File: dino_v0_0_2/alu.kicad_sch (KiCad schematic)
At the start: 20 parts, among them U38 74F382N, U40 74F382N, U45 74LS373, U46 74LS373, U47 74LS373, U48 74LS157, U49 74LS273, U50 74LS02, U52 74LS02, U53 74LS08

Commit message: feat: Phase F/F+ ISA: 174 instructions, timing fixes, and robust tooling
This commit integrates Phase F and F+ of the ISA, expanding the instruction set to 174 instructions. This includes:
- New conditional branch `JNC`, register-to-register moves, SP/PC readbacks and manipulation (HLSP/SPHL, INXSP/DCXSP).
- Indexed memory access (LDAX/STAX), SP-relative memory access (LDAS/STAS), and memory-indirect addressing (LDAM/STAM/JMPM, etc.) as a new addressing mode.
- Immediate ALU operations (ADI, SUI, ANI, etc.) and ALU results directly to B/C or memory.
- Compare-only instructions (CMP, TST).
- The `IN` opcode has been fully retired from the ISA as of 2026-08-27, and `0x00` confirmed as `NOP`.

Crucially, this commit resolves several critical hardware stability issues:
- Eliminated random machine halts by replacing a damaged `74HC14` (`U56`) and rewiring the reset chain.
- Fixed intermittent failures in `PROG_isasoak` due to ground bounce by starring GND/VCC connections (2026-09-01).
- Introduced microcode-level "SETTLE" states for 23 ALU instructions to ensure timing margins at 1.024MHz, resolving timing-dependent failures for instructions that load and consume operands in consecutive T-states.

The development tooling has also been significantly improved for robustness and accuracy:
- The assembler (`asm.py`) now uses `microcode_gen.py` as the single source of truth for ISA definitions.
- New self-checking ISA tests (`PROG_isa` and variants) were developed, incorporating mutation testing to verify subtest efficacy and provide detailed diagnostic feedback for debugging marginality or hangs.
- The microcode generator enforces hardware constraints at build time (e.g., valid `cond` flag selections, preventing `src=ROM` `dst=RAM` conflicts that led to the `MVI` bug).
- The simulator (`progrom_gen.py`) accurately models `OUT` latching the bus and `dst=RAM` writing to the address bus, and refuses to guess undefined `FLAG_C` states after logic operations.
- The root `Makefile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
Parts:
- added C82: 0.1µF, symbol Device:C_Small
- added U77: 74LS157, symbol 74xx:74LS157
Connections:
- net +5V: now also C82.1, U77.16 (VCC)
- net FLAG_C: now also U77.2 (I0a)
- net FLAG_Z: now also U77.3 (I1a)
- net GND: now also C82.2, U77.10 (I1c), U77.11 (I0c), U77.13 (I1d), U77.14 (I0d), U77.15 (E), U77.5 (I0b), U77.6 (I1b), U77.8 (GND)
- new net COND_FLAG: U77.4 (Za)
- new net CW21: U77.1 (S)
- no-connect marks 6 -> 9
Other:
- moved on the sheet: U38, U45, U47

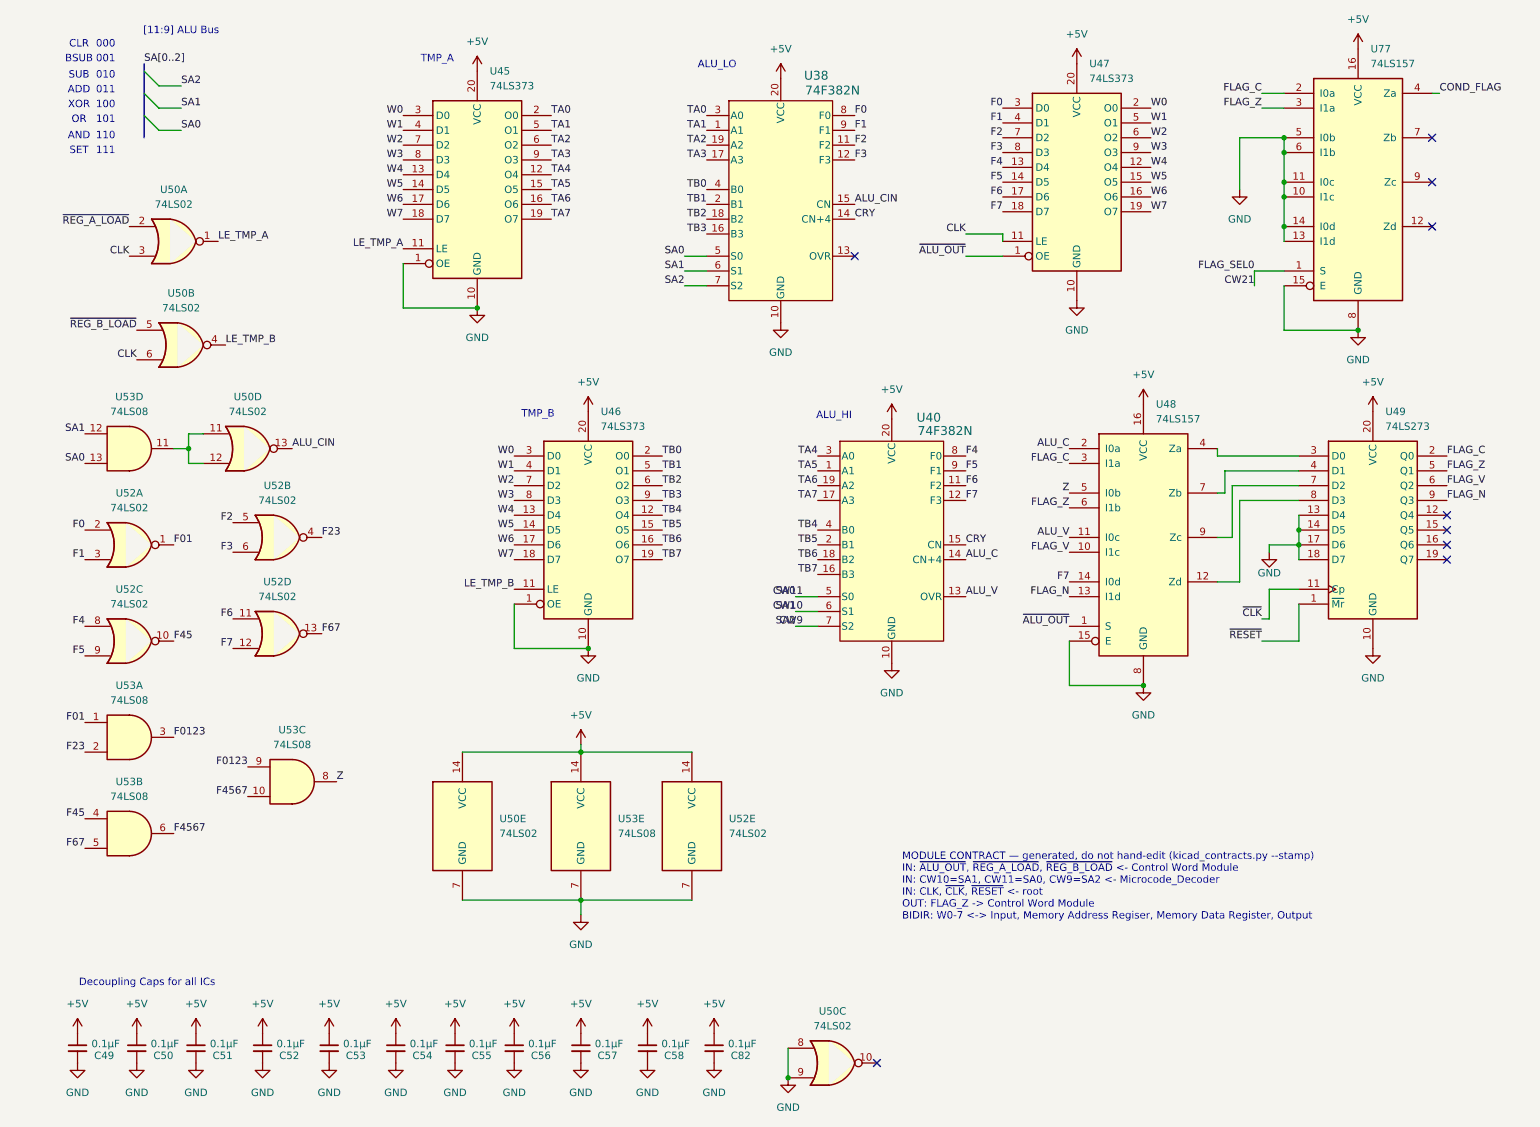
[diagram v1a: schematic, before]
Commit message: feat(kicad): footprints, power sheet, global labels, PCB draft
Every symbol gets a stock THT footprint (plain DIP, no sockets, so the
3D render shows ICs). New Power sheet: 24-pin ATX header for a picoPSU,
rails +5V/+3.3V/+12V/-12V/GND only; no -5V exists on any ATX unit since
2003, none drawn. PS_ON# on a 2-pin header.

Cross-sheet labels become global labels. KiCad joined nothing between
sheets before: 122 base names were split per sheet, ERC saw 90 undriven
inputs whose driver sat one sheet away, and the PCB ratsnest stopped at
every sheet boundary. Proof: KiCad's netlist after equals a name-join of
its netlist before plus the 15 CW alias pairs, pin for pin.

kicad_contracts took a node's sheet from the net name's /Sheet/ prefix;
global nets have none, so it emitted an empty contracts doc. Sheet now
comes from the component's own path; the doc regenerates with zero diff.

ERC 477 -> 2. Real fixes: ROM I/O pins input -> tri_state, '382 GND pin
power_out -> power_in, four orphan symbols rehomed to project lib `dino`,
one stub wire. 133 by-design warnings excluded by uuid ('245 readback on
counter Q, alias stubs, probe-point labels); the two left are bus
signals the peripheral bus sheet will consume.

PCB draft: 198 footprints placed per sheet, all pads netted, no tracks.

Co-Authored-By: Claude Fable 5.1 <noreply@anthropic.com>
Claude-Session: https://claude.ai/code/session_018irreFHb1xEykW5kCD26ow
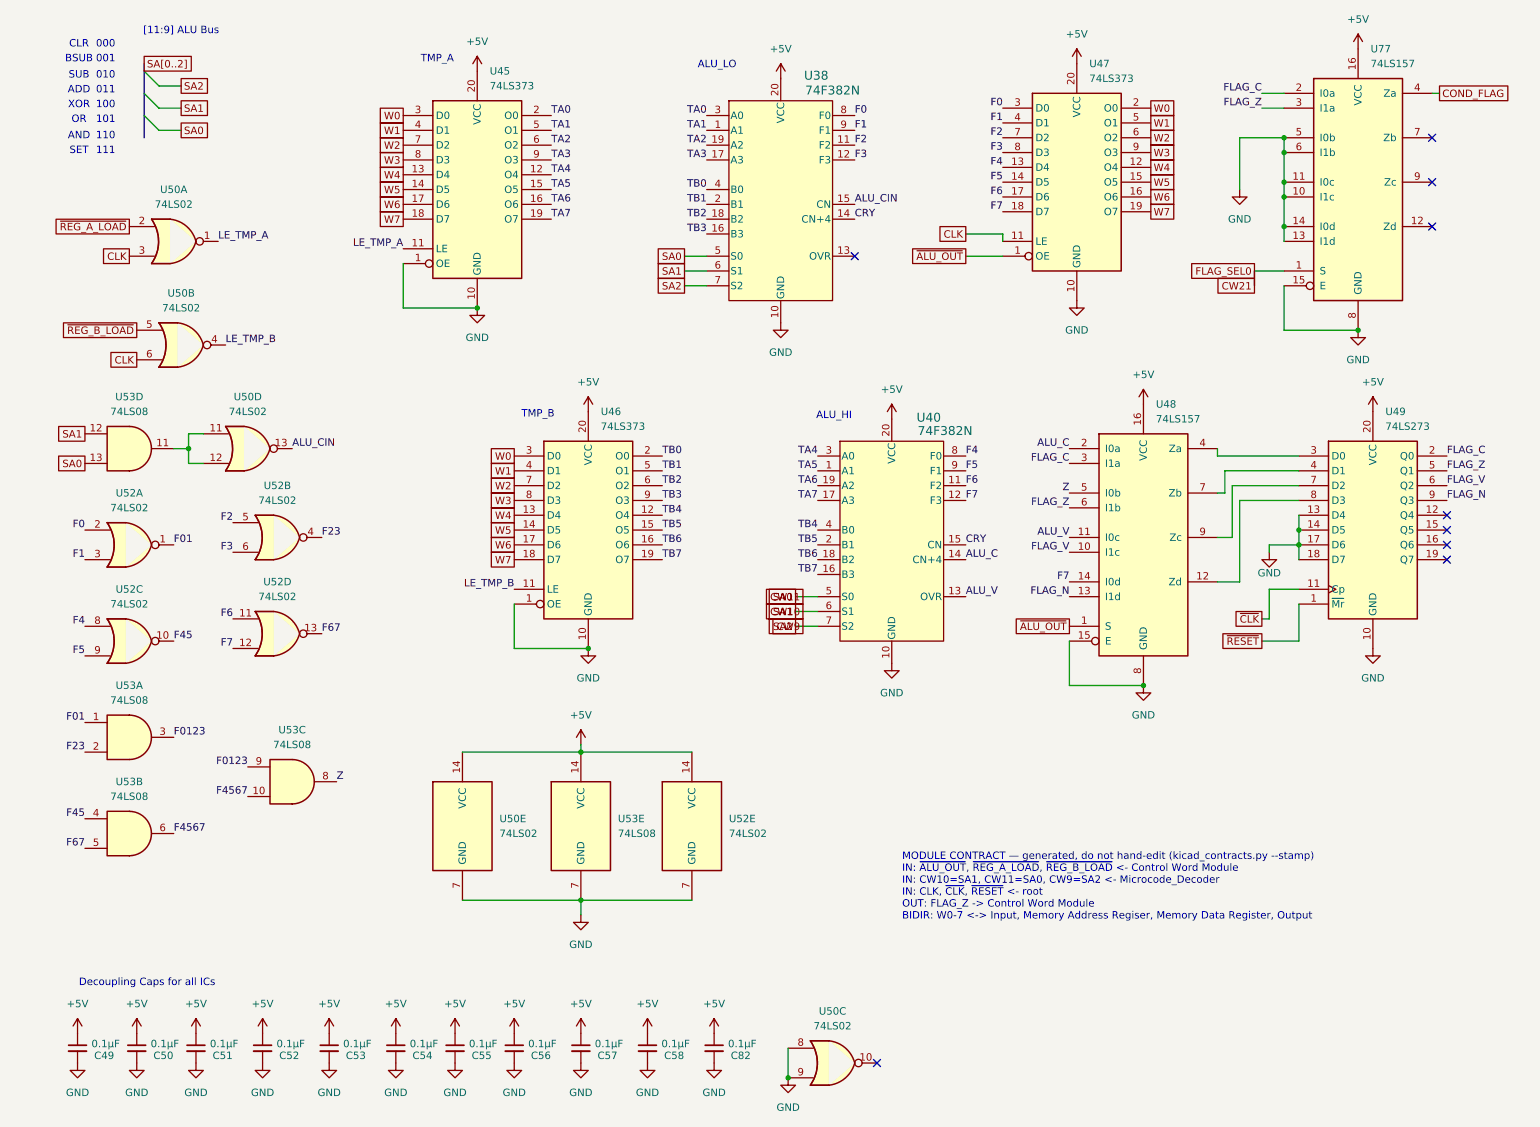
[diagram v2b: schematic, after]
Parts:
- C49, C50, C51, C52, C53, C54, C55, C56, C57, C58, C82: footprint (none) -> Capacitor_THT:C_Disc_D5.0mm_W2.5mm_P2.50mm
- U38, U40: footprint PDIP20_26P42X6P6_ONS -> Package_DIP:DIP-20_W7.62mm
- U45, U46, U47, U49: footprint (none) -> Package_DIP:DIP-20_W7.62mm
- U48, U77: footprint (none) -> Package_DIP:DIP-16_W7.62mm
- U50, U52, U53: footprint (none) -> Package_DIP:DIP-14_W7.62mm
